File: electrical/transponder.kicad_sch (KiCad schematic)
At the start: 4 parts

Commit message: Interim check-in
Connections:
- net ADSB2_SERIAL_IN is gone; now on net ADSB1_SERIAL_IN: GDL52.DSUB_6 (RS-232_RX_2)
- net ADSB2_SERIAL_OUT is gone; now on net ADSB1_SERIAL_OUT: GDL52.DSUB_5 (RS-232_TX_2)
- net MUSIC_OUT_LEFT is gone; now on net ADSB1_SERIAL_IN: GDL52.DSUB_13 (MUSIC_OUT_LEFT)
- net MUSIC_OUT_LO is gone; now on net ADSB1_SERIAL_GND: GDL52.DSUB_14 (MUSIC_OUT_LO)
- net MUSIC_OUT_RIGHT is gone; now on net ADSB1_SERIAL_OUT: GDL52.DSUB_15 (MUSIC_OUT_RIGHT)
- net GND: no longer GTX320.P102_25 (SIGNAL_GROUND)
- net LIGHTING_HI: now also GTX320.P102_24 (14V_LIGHTING); no longer GTX320.P102_23 (28V_LIGHTING)
- new net AIRDATA_RS232_GND: GTX320.P102_25 (SIGNAL_GROUND)
- no-connect marks 4 -> 7

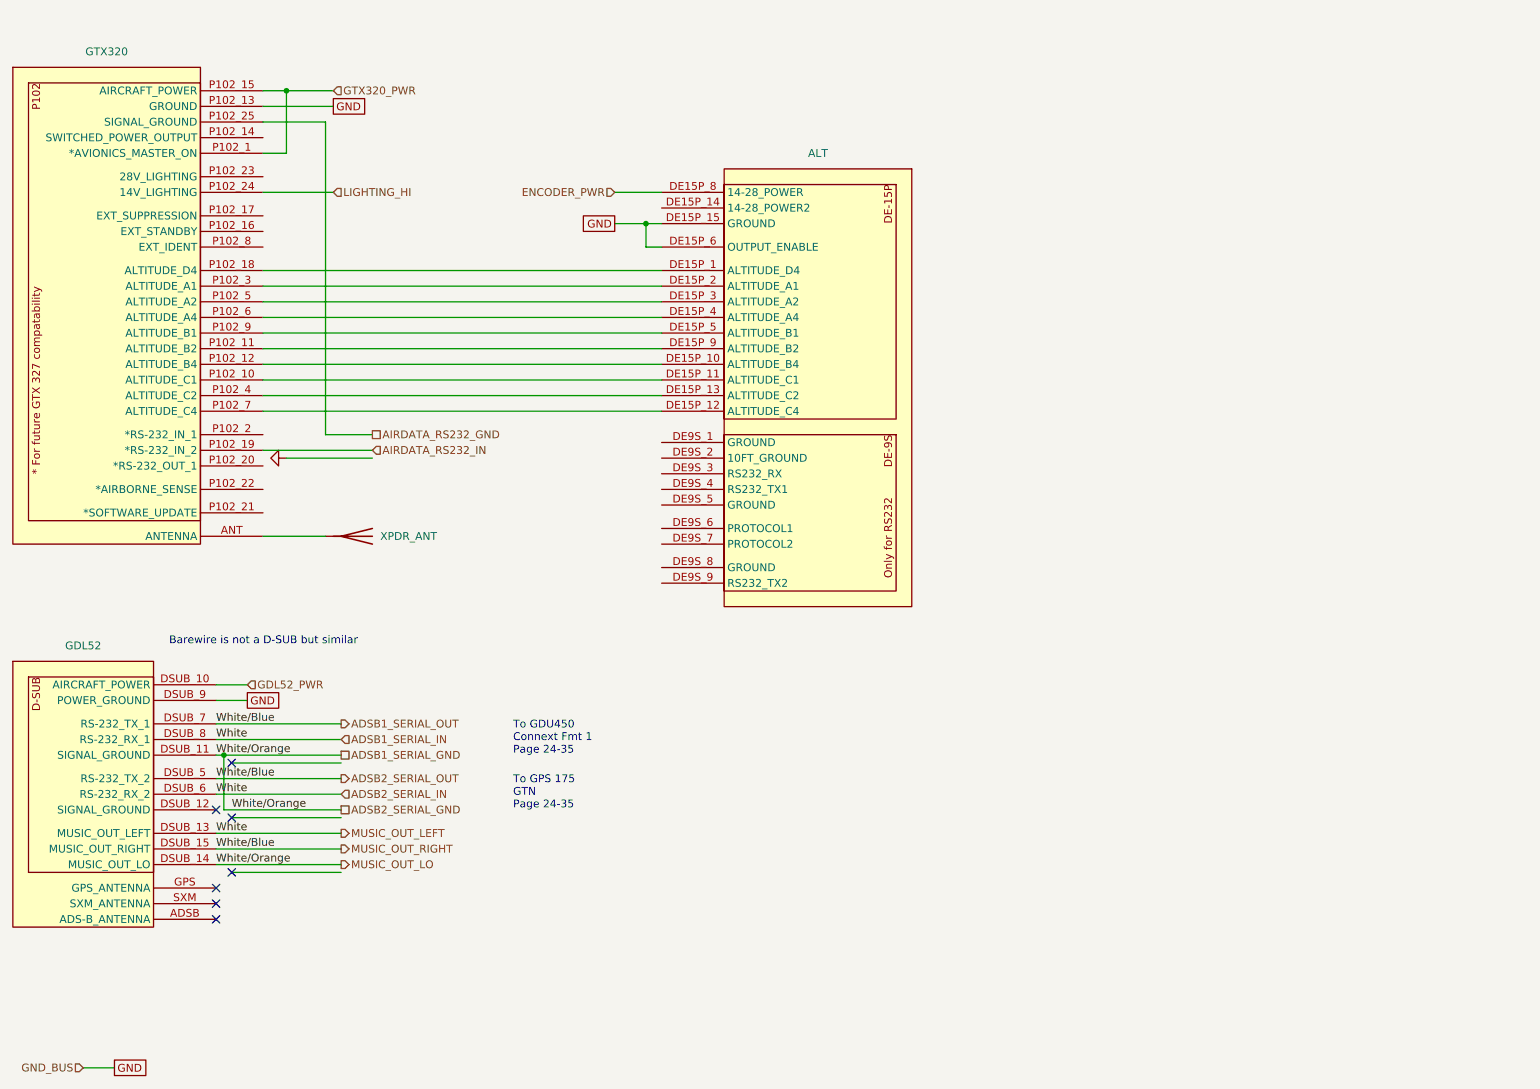
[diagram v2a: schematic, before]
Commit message: Went through and changed a lot from discussions and tradeoffs. Added GTX 330, rmemoved Connext from GDU and added to GPS 175 from GDL 52. Added relay for smoke and to not use GAD 27. Added Tach sensor for SureFly. Added carb heat. Added connectors to run panel disconnected.
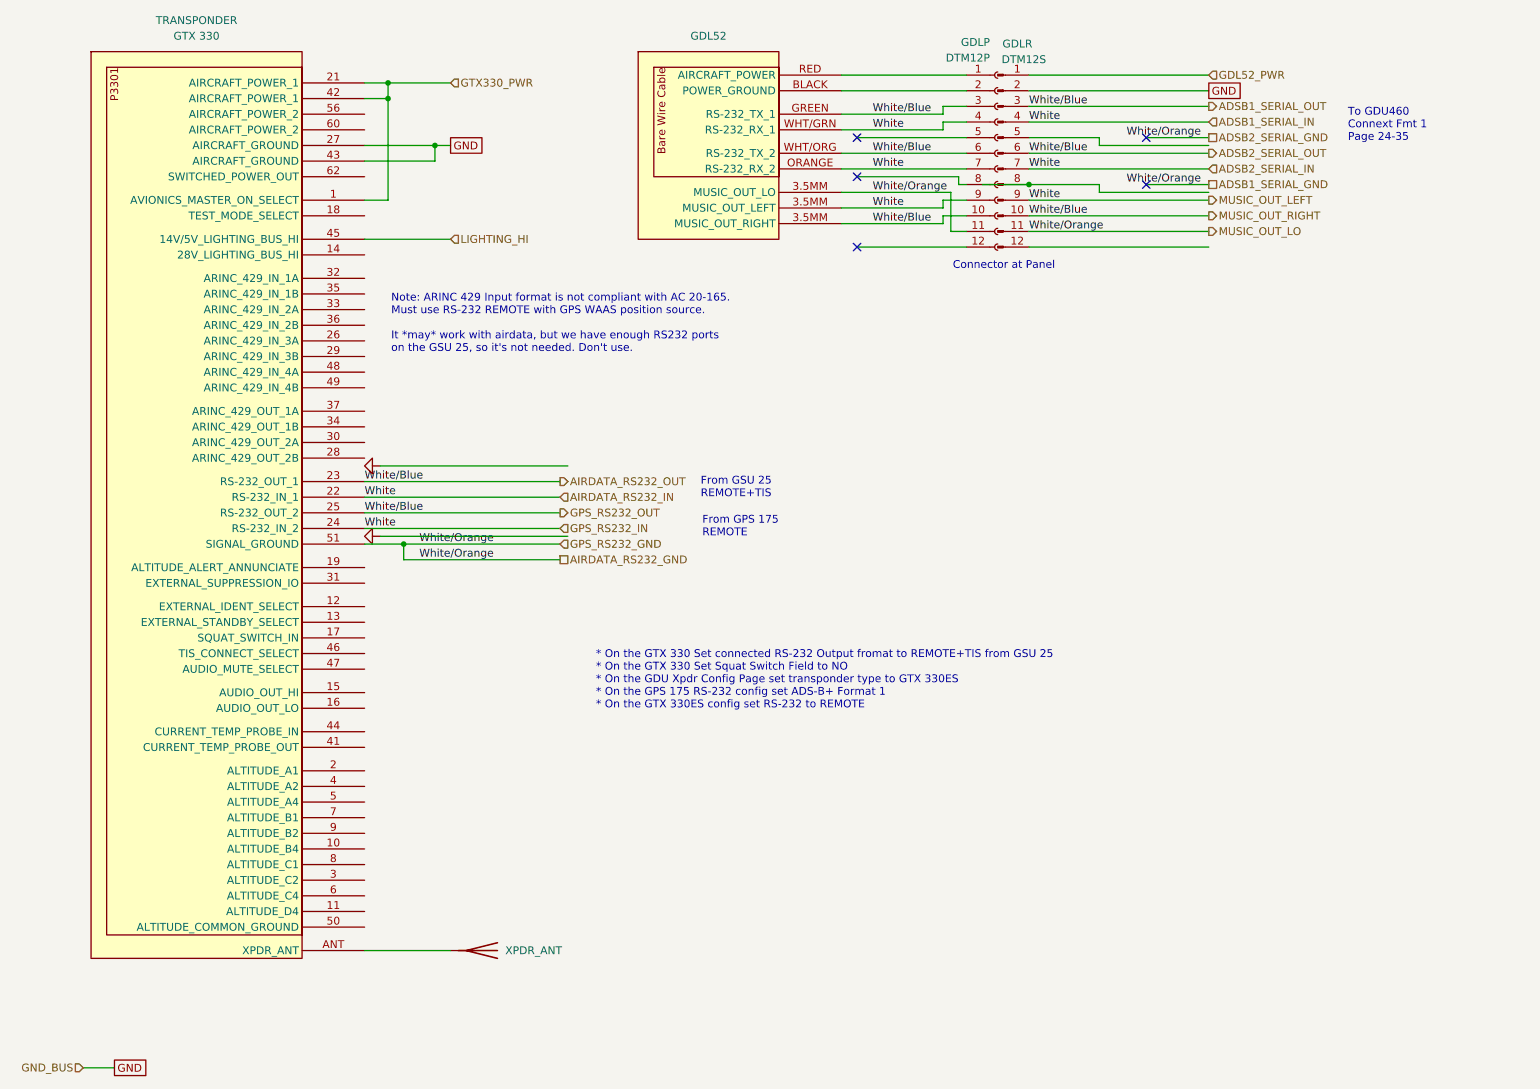
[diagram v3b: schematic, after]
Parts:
- removed ALT: ~, symbol flyerx:TransCal_SSD120-30N
- removed GDL52: ~, symbol flyerx:Garmin_GDL52R
- removed GTX320: ~, symbol flyerx:Garmin_GTX320
- added GDL52: ~, symbol flyerx:Garmin_GDL52
- added GDLP: DTM12P, symbol Connector:Conn_01x12_Socket
- added GDLR: DTM12S, symbol Connector:Conn_01x12_Pin
- added TRANSPONDER: GTX 330, symbol flyerx:Garmin_GTX330
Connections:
- net ADSB1_SERIAL_GND: now also GDL52.3.5MM (MUSIC_OUT_RIGHT), GDLP.11 (Pin_11), GDLR.11 (Pin_11), TRANSPONDER.51 (SIGNAL_GROUND)
- net ADSB1_SERIAL_IN: now also GDL52.3.5MM (MUSIC_OUT_RIGHT), GDL52.ORANGE (RS-232_RX_2), GDL52.WHT/GRN (RS-232_RX_1), GDLP.4 (Pin_4), GDLP.7 (Pin_7), GDLP.9 (Pin_9), GDLR.4 (Pin_4), GDLR.7 (Pin_7), GDLR.9 (Pin_9), TRANSPONDER.22 (RS-232_IN_1), TRANSPONDER.24 (RS-232_IN_2)
- net ADSB1_SERIAL_OUT: now also GDL52.3.5MM (MUSIC_OUT_RIGHT), GDL52.GREEN (RS-232_TX_1), GDL52.WHT/ORG (RS-232_TX_2), GDLP.10 (Pin_10), GDLP.3 (Pin_3), GDLP.6 (Pin_6), GDLR.10 (Pin_10), GDLR.3 (Pin_3), GDLR.6 (Pin_6), TRANSPONDER.23 (RS-232_OUT_1), TRANSPONDER.25 (RS-232_OUT_2)
- net GDL52_PWR: now also GDLR.1 (Pin_1)
- net GND: now also GDLR.2 (Pin_2), TRANSPONDER.27 (AIRCRAFT_GROUND), TRANSPONDER.43 (AIRCRAFT_GROUND)
- net LIGHTING_HI: now also TRANSPONDER.45 (14V/5V_LIGHTING_BUS_HI)
- net at XPDR_ANT.1 (A): now also TRANSPONDER.ANT (XPDR_ANT)
- new net: GDL52.BLACK (POWER_GROUND), GDLP.2 (Pin_2)
- new net: GDL52.RED (AIRCRAFT_POWER), GDLP.1 (Pin_1)
- new net GTX330_PWR: TRANSPONDER.1 (AVIONICS_MASTER_ON_SELECT), TRANSPONDER.21 (AIRCRAFT_POWER_1), TRANSPONDER.42 (AIRCRAFT_POWER_1)
- no-connect marks 7 -> 5
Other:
- note added: "* On the GTX 330 Set connected RS-232 Output fromat to REMOTE+TIS from GSU 25 * On the GTX 330 Set Squat Switch Field to NO * On the GDU Xpdr Config Page set transponder type to GTX 330ES * On the GPS 175 RS-232 config set ADS-B+ Format 1 * On the GTX 330ES config set RS-232 to REMOTE"
- note added: "Connector at Panel"
- note added: "From GPS 175 REMOTE"
- note added: "From GSU 25 REMOTE+TIS"
- note added: "Note: ARINC 429 Input format is not compliant with AC 20-165. Must use RS-232 REMOTE with GPS WAAS position source. It *may* work with airdata, but we have enough RS232 ports on the GSU 25, so it's not needed. Don't use."
- note added: "To GDU460 Connext Fmt 1 Page 24-35"
- note removed: "Barewire is not a D-SUB but similar"
- note removed: "To GDU450 Connext Fmt 1 Page 24-35"
- note removed: "To GPS 175 GTN Page 24-35"
- moved on the sheet: XPDR_ANT

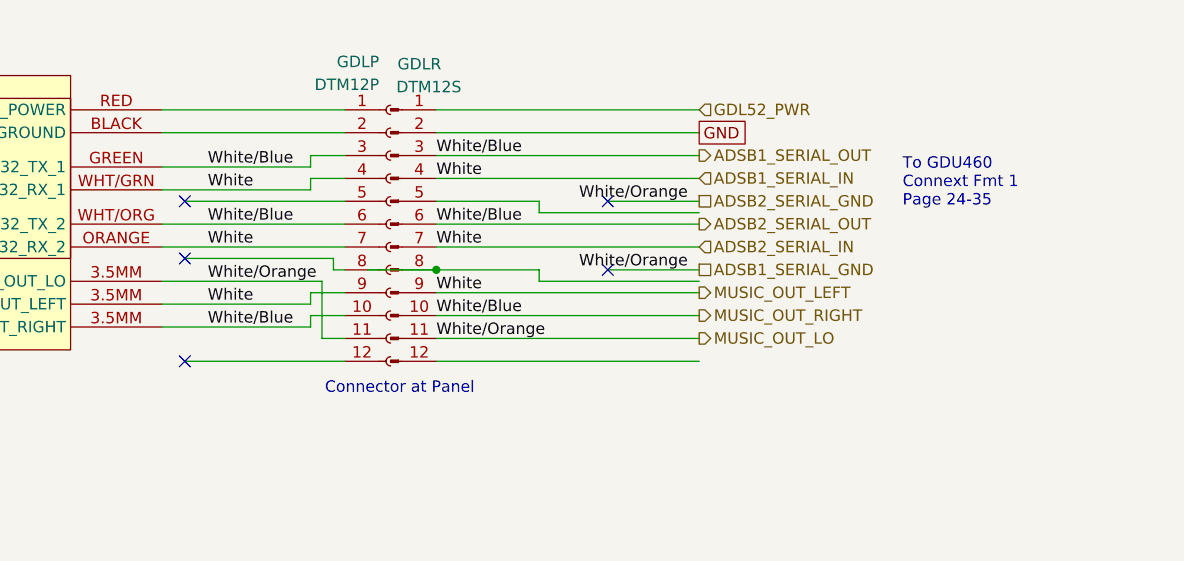
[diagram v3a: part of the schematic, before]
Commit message: Added extra connector for GDL 52, rewired stick to have flaps up/down instead of level/smoke. Put smoke on panel.
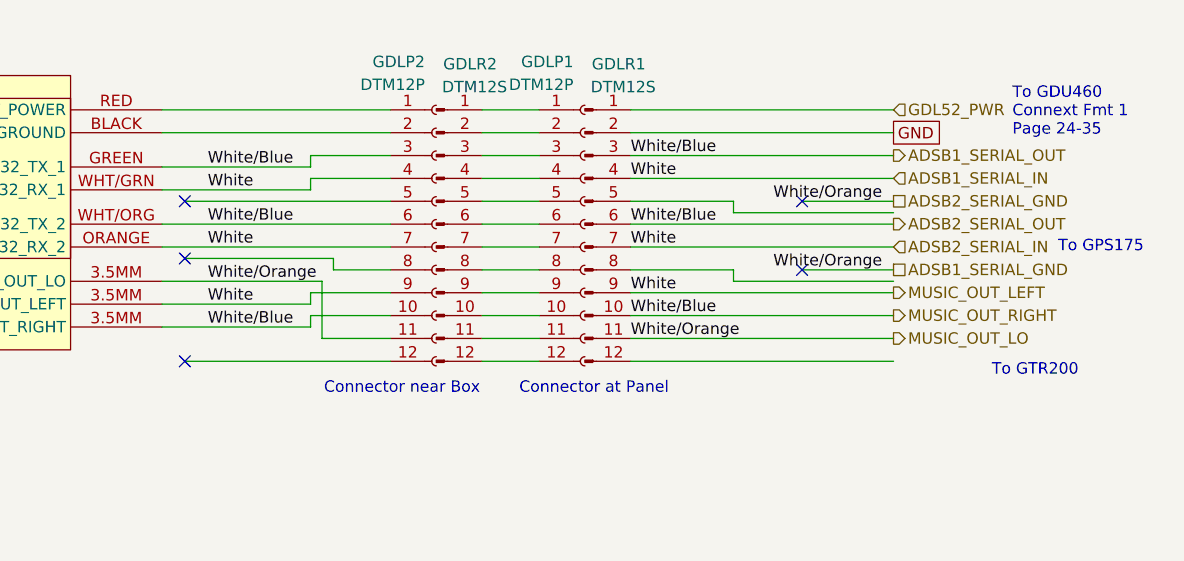
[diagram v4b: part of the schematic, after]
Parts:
- added GDLP2: DTM12P, symbol Connector:Conn_01x12_Socket
- added GDLR2: DTM12S, symbol Connector:Conn_01x12_Pin
- renumbered GDLP to GDLP1, GDLR to GDLR1
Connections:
- net ADSB1_SERIAL_GND: now also GDLP2.11 (Pin_11); no longer GDLP1.11 (Pin_11)
- net ADSB1_SERIAL_IN: now also GDLP2.4 (Pin_4), GDLP2.7 (Pin_7), GDLP2.9 (Pin_9); no longer GDLP1.4 (Pin_4), GDLP1.7 (Pin_7), GDLP1.9 (Pin_9)
- net ADSB1_SERIAL_OUT: now also GDLP2.10 (Pin_10), GDLP2.3 (Pin_3), GDLP2.6 (Pin_6); no longer GDLP1.10 (Pin_10), GDLP1.3 (Pin_3), GDLP1.6 (Pin_6)
- net at GDL52.BLACK (POWER_GROUND): now also GDLP2.2 (Pin_2); no longer GDLP1.2 (Pin_2)
- net at GDL52.RED (AIRCRAFT_POWER): now also GDLP2.1 (Pin_1); no longer GDLP1.1 (Pin_1)
- net at GDLP1.12 (Pin_12): now also GDLR2.12 (Pin_12)
- net at GDLP1.5 (Pin_5): now also GDLR2.5 (Pin_5)
- net at GDLP1.8 (Pin_8): now also GDLR2.8 (Pin_8)
- new net: GDLP1.1 (Pin_1), GDLR2.1 (Pin_1)
- new net: GDLP1.10 (Pin_10), GDLR2.10 (Pin_10)
- new net: GDLP1.11 (Pin_11), GDLR2.11 (Pin_11)
- new net: GDLP1.2 (Pin_2), GDLR2.2 (Pin_2)
- new net: GDLP1.3 (Pin_3), GDLR2.3 (Pin_3)
- new net: GDLP1.4 (Pin_4), GDLR2.4 (Pin_4)
- new net: GDLP1.6 (Pin_6), GDLR2.6 (Pin_6)
- new net: GDLP1.7 (Pin_7), GDLR2.7 (Pin_7)
- new net: GDLP1.9 (Pin_9), GDLR2.9 (Pin_9)
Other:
- note added: "Connector near Box"
- note added: "To GPS175"
- note added: "To GTR200"
- moved on the sheet: GDLP1, GDLR1

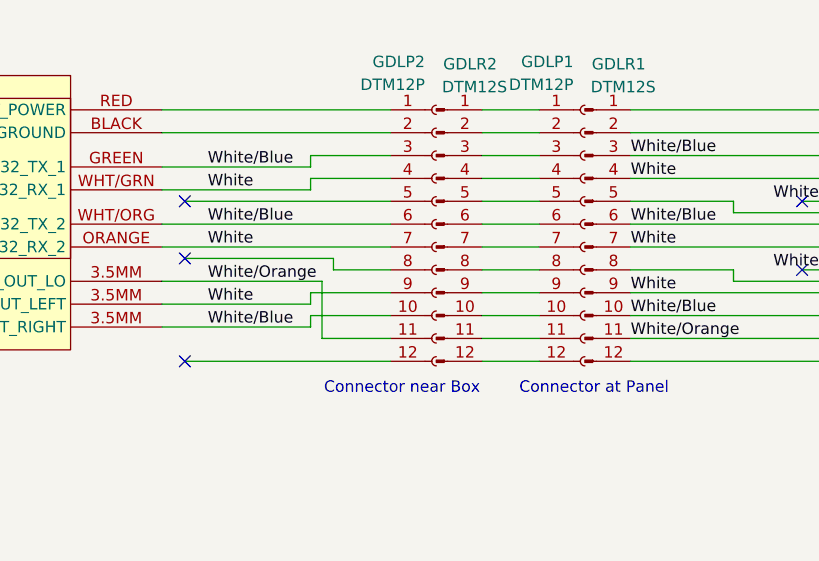
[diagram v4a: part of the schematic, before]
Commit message: Fixed can hi pin on GTR 20. Changed how ACX-BT wires with low vs. shield. Added pitch trim colors. Removed pitch trim ground going to flaps ground. Removed extra connector on GDL 52 and changed to 4 wire shielded instead of two 2 wire shielded.
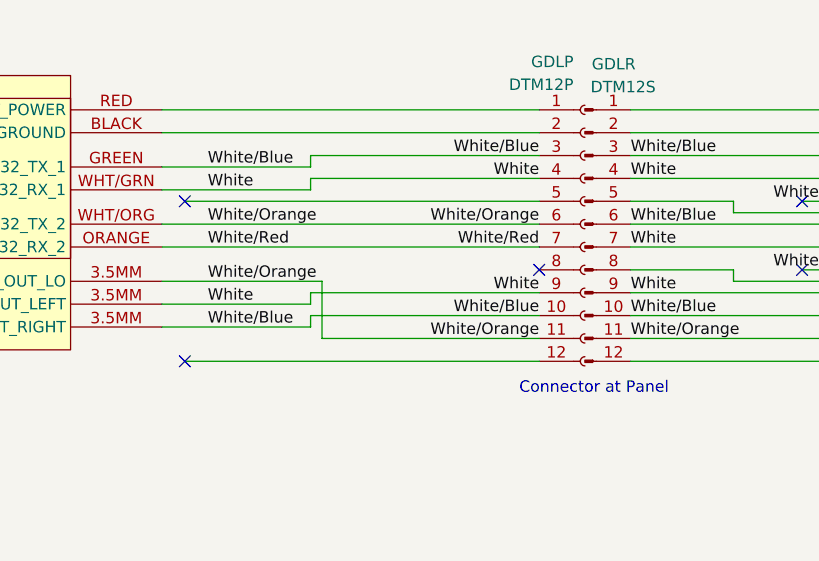
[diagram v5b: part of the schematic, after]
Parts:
- removed GDLP2: DTM12P, symbol Connector:Conn_01x12_Socket
- removed GDLR2: DTM12S, symbol Connector:Conn_01x12_Pin
- renumbered GDLP1 to GDLP, GDLR1 to GDLR
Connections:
- net ADSB1_SERIAL_GND: now also GDL52.WHT/ORG (RS-232_TX_2), GDLP.11 (Pin_11), GDLP.6 (Pin_6)
- net ADSB1_SERIAL_IN: now also GDLP.4 (Pin_4), GDLP.9 (Pin_9); no longer GDL52.ORANGE (RS-232_RX_2)
- net ADSB1_SERIAL_OUT: now also GDLP.10 (Pin_10), GDLP.3 (Pin_3); no longer GDL52.WHT/ORG (RS-232_TX_2)
- net at GDL52.BLACK (POWER_GROUND): now also GDLP.2 (Pin_2)
- net at GDL52.RED (AIRCRAFT_POWER): now also GDLP.1 (Pin_1)
- net White/Red: now reaches GDLP.7 (Pin_7)
- net White/Red: now also GDL52.ORANGE (RS-232_RX_2)
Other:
- note removed: "Connector near Box"

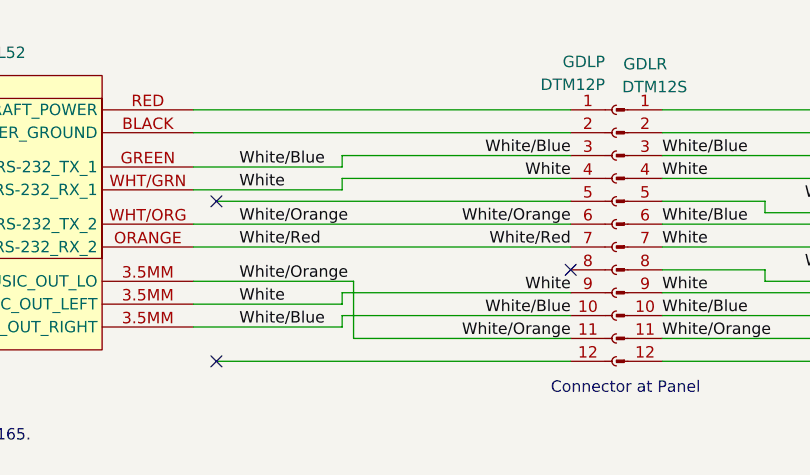
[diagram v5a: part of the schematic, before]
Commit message: Changed GDL to be a 4 wire
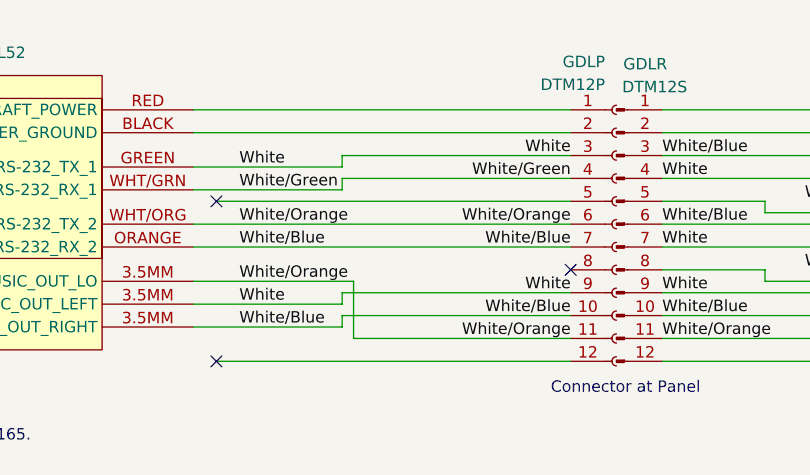
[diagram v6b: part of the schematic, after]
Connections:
- net White/Red is gone; now on net ADSB1_SERIAL_OUT: GDL52.ORANGE (RS-232_RX_2), GDLP.7 (Pin_7)
- net ADSB1_SERIAL_IN: now also GDL52.GREEN (RS-232_TX_1), GDLP.3 (Pin_3); no longer GDL52.WHT/GRN (RS-232_RX_1), GDLP.4 (Pin_4)
- net ADSB1_SERIAL_OUT: no longer GDL52.GREEN (RS-232_TX_1), GDLP.3 (Pin_3)
- new net White/Green: GDL52.WHT/GRN (RS-232_RX_1), GDLP.4 (Pin_4)
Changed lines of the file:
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@@
 	(title_block
 		(title "Transponder")
-		(date "2026-01-13")
-		(rev "1.2.11")
+		(date "2026-01-15")
+		(rev "1.2.13")
 		(company "N877RV")
 	)
@@
 		)
 	)
-	(label "White{slash}Blue"
+	(label "White"
 		(at 200.66 29.21 180)
 		(effects
@@
 		)
 	)
-	(label "White{slash}Red"
+	(label "White{slash}Blue"
 		(at 200.66 39.37 180)
 		(effects
@@
 		)
 	)
-	(label "White"
+	(label "White{slash}Green"
 		(at 163.83 33.02 0)
 		(effects
@@
 		)
 	)
-	(label "White{slash}Blue"
+	(label "White"
 		(at 163.83 30.48 0)
 		(effects
@@
 		)
 	)
-	(label "White{slash}Red"
+	(label "White{slash}Blue"
 		(at 163.83 39.37 0)
 		(effects
@@
 		)
 	)
-	(label "White"
+	(label "White{slash}Green"
 		(at 200.66 31.75 180)
 		(effects

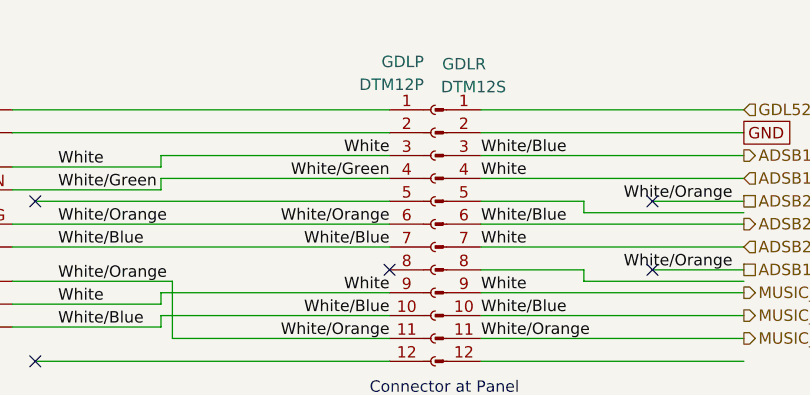
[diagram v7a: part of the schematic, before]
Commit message: Fixed GDL 52 power color
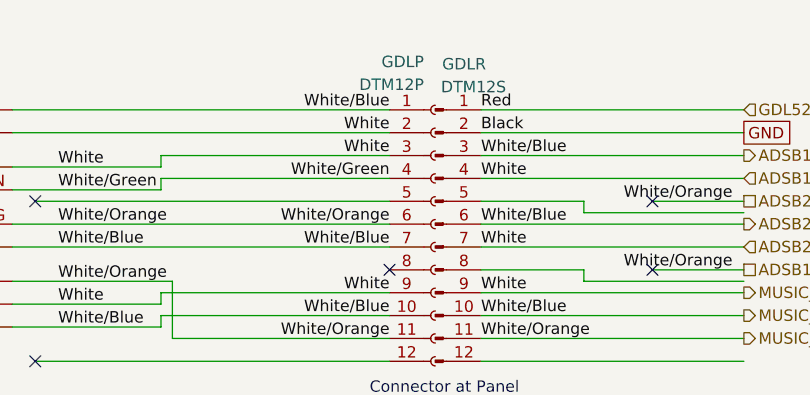
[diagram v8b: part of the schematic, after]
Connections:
- net ADSB1_SERIAL_IN: now also GDL52.BLACK (POWER_GROUND), GDLP.2 (Pin_2)
- net ADSB1_SERIAL_OUT: now also GDL52.RED (AIRCRAFT_POWER), GDLP.1 (Pin_1)
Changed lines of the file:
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@@
+		)
+	)
+	(label "White"
+		(at 200.66 26.67 180)
+		(effects
+			(font
+				(size 1.27 1.27)
+			)
+			(justify right bottom)
 		)
 	)
@@
 		)
 	)
+	(label "Red"
+		(at 210.82 24.13 0)
+		(effects
+			(font
+				(size 1.27 1.27)
+			)
+			(justify left bottom)
+		)
+	)
+	(label "Black"
+		(at 210.82 26.67 0)
+		(effects
+			(font
+				(size 1.27 1.27)
+			)
+			(justify left bottom)
+		)
+	)
 	(label "White{slash}Green"
 		(at 200.66 31.75 180)
@@
 		)
 	)
+	(label "White{slash}Blue"
+		(at 200.66 24.13 180)
+		(effects
+			(font
+				(size 1.27 1.27)
+			)
+			(justify right bottom)
+		)
+	)
